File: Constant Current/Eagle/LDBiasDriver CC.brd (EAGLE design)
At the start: 44.8 x 22.9 mm, 24 parts, among them IC1 MCP1703-5002E/DB, IC2 MLD203P1, IC3 LM358D

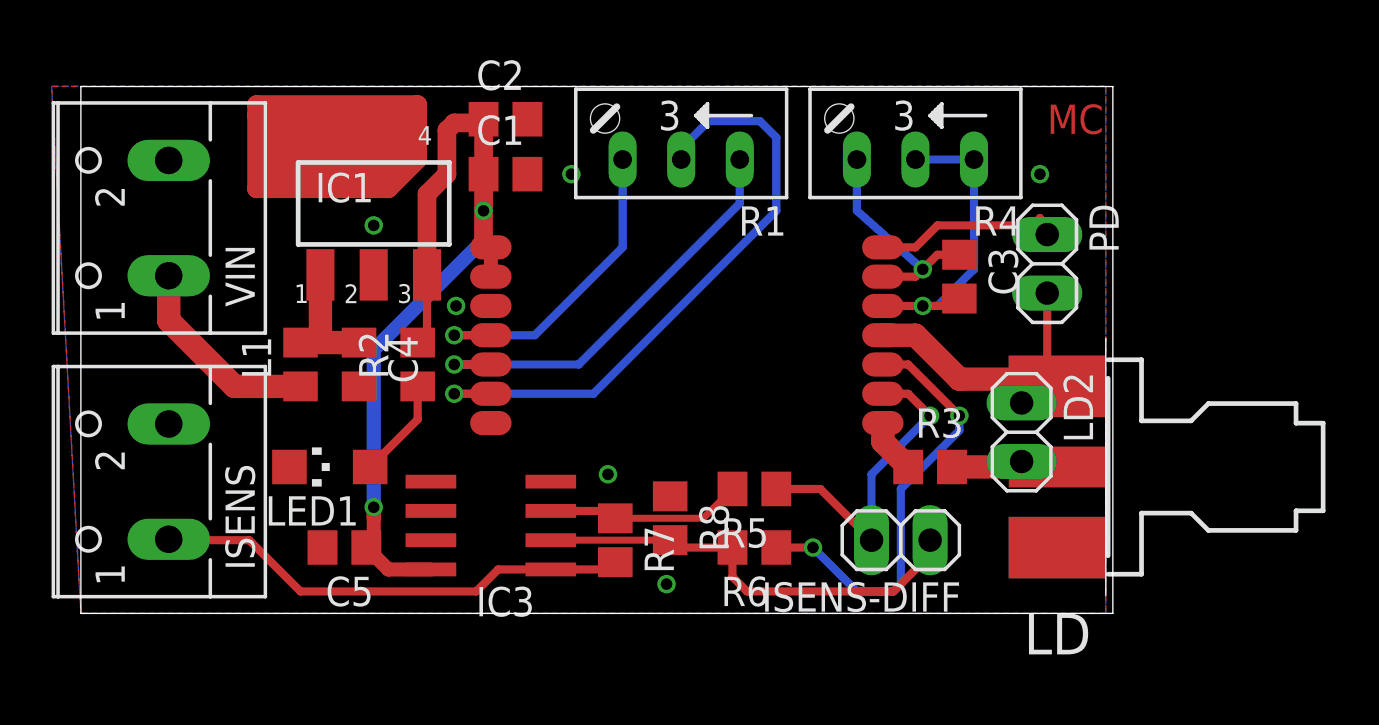
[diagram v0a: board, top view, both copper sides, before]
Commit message: Added a CC version
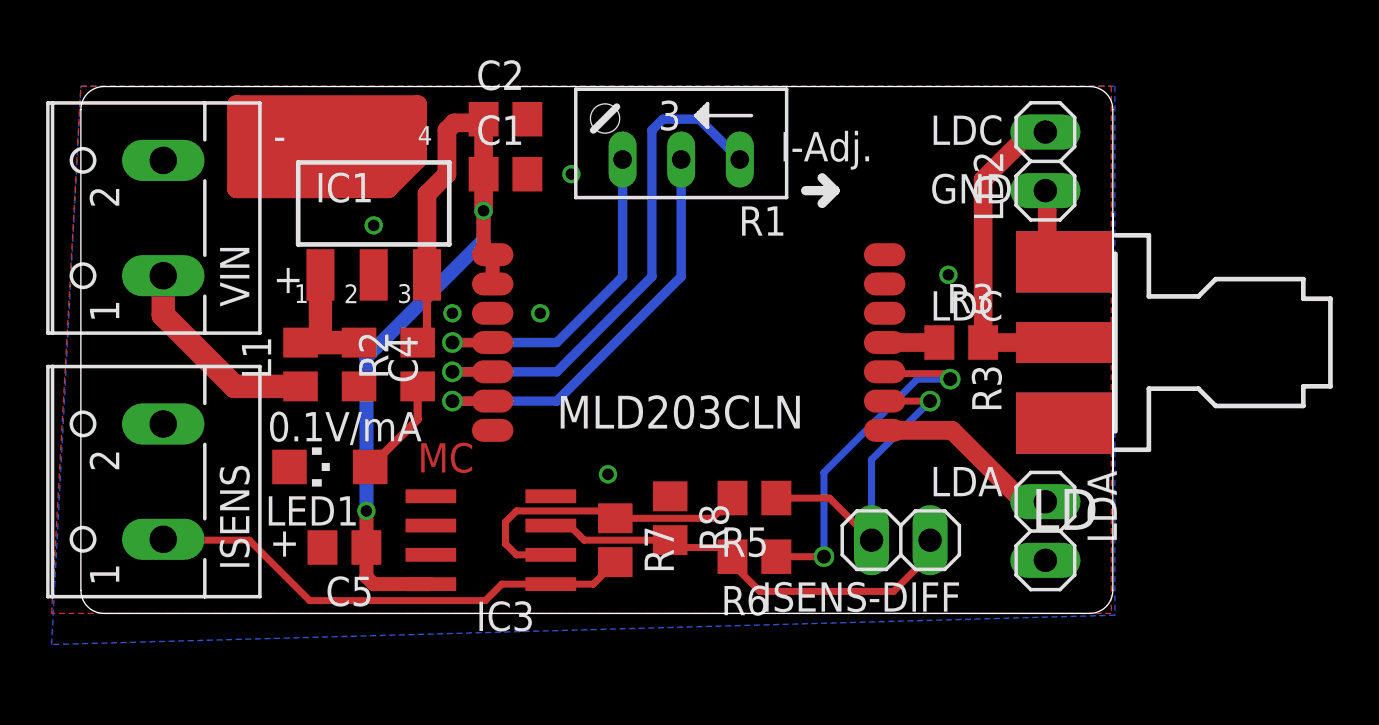
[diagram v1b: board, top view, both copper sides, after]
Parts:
- removed C3: 100pF, rcl:C0805
- removed IC2: MLD203P1, laser diode:MLD203
- removed PD: (no value), pinhead:1X02
- removed R4: 100k, pot:RJ9W
- added LDA: (no value), pinhead:1X02
- added U$1: MLD203CLN, laser diode:MLD203
- moved LD2 11.8 mm to (41.8, 19.6), turned to 90 degrees
- moved R3 5.56 mm to (38.2, 11.7)
- moved LD 5.41 mm to (44.8, 11.7)
- moved IC3 0.64 mm to (17.8, 3.17)
- moved R6 0.40 mm to (29.2, 2.46)
- moved R5 0.40 mm to (29.2, 5.00)
- moved ISENS 0.24 mm to (2.30, 5.71)
- moved VIN 0.24 mm to (2.30, 17.1)
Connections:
- removed net N$10: IC2.P$11, LD.G@1, LD.G@2, LD.G@3, LD.G@4, LD2.1, PD.2
- removed net N$12: C3.2, IC2.P$10, R4.E, R4.S
- removed net N$13: C3.1, IC2.P$9, R4.A
- net +5V: now also U$1.P$1, U$1.P$2; no longer IC2.P$1, IC2.P$2
- net GND: now also LD.G@1, LD.G@2, LD.G@3, LD.G@4, LD2.1, LDA.2, U$1.P$3; no longer IC2.P$3
- net N$11: now also LDA.1, U$1.P$14; no longer IC2.P$8, PD.1
- net N$16: now also IC3.2; no longer IC3.3
- net N$17: now also IC3.3; no longer IC3.2
- net N$2: now also R1.E, U$1.P$5; no longer IC2.P$6, R1.S
- net N$4: now also R1.S, U$1.P$6; no longer IC2.P$5, R1.E
- net N$5: now also U$1.P$4; no longer IC2.P$4
- net N$6: now also U$1.P$12; no longer IC2.P$12
- net N$7: now also U$1.P$13; no longer IC2.P$13
- net N$9: now also U$1.P$11; no longer IC2.P$14
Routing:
- net N$10: track 18.8 -> 0.00 mm
- net N$12: track 13.6 -> 0.00 mm, vias 1 -> 0
- net N$13: track 9.76 -> 0.00 mm, vias 1 -> 0
- net N$8: track 6.43 -> 14.1 mm
- net N$16: track 8.48 -> 13.7 mm
- net N$2: track 27.4 -> 23.2 mm
- net GND: track 0.00 -> 3.92 mm
- net N$6: track 18.9 -> 15.8 mm
- net N$1: track 26.9 -> 29.5 mm
- net N$19: track 22.1 -> 24.2 mm
- net +5V: track 38.9 -> 40.0 mm
- net N$5: track 14.3 -> 15.4 mm
- net N$17: track 19.5 -> 20.2 mm
- net N$18: track 20.8 -> 21.4 mm
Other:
- outline, holes or cut-outs redrawn
- board text added: "+"
- board text added: "-"
- board text added: "0.1V/mA"
- board text added: "0.1V/mA+"
- board text added: "6-12V+"
- board text added: "I-Adj."
- board text added: "LD Bias CC"
- board text added: "LDC"
- board text added: "MLD203CLN"
- board text removed: "0.1V/mA +"
- board text removed: "6-12V +"
- board text removed: "LD Bias"
- board text removed: "PDA"
- board text removed: "Power"
